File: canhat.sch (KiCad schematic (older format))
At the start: 27 parts, among them J1 Raspberry_Pi_2_3, J2 CAN In/Out/GND, J3 5V, U1 MCP2515-xSO, U2 SN65HVD234, U3 AT24C32-SSHM, Y1 16MHz

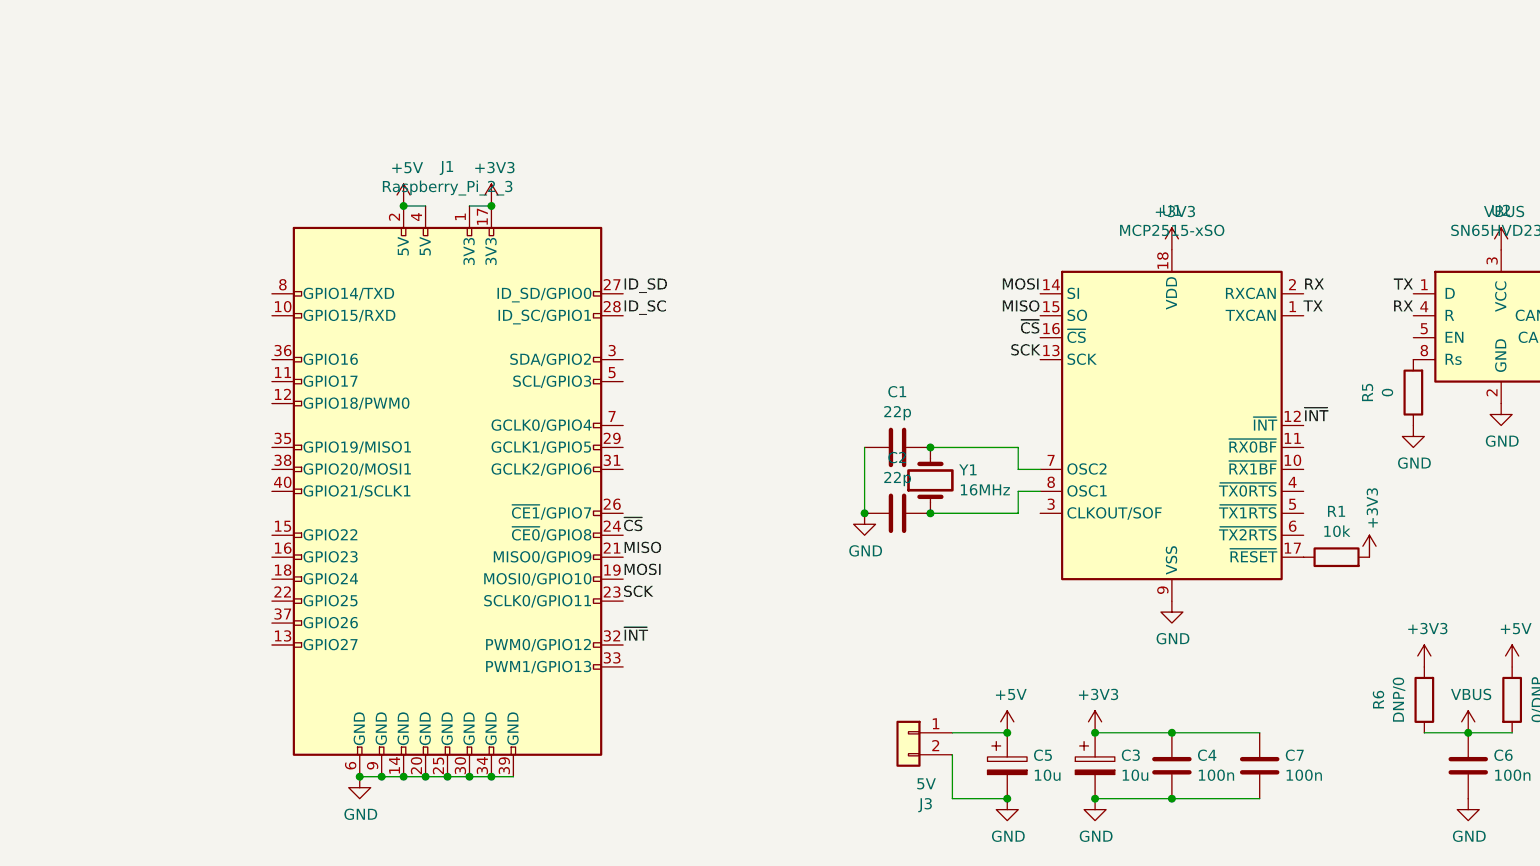
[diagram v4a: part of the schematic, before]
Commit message: Added protective resistors between xceiver and controller
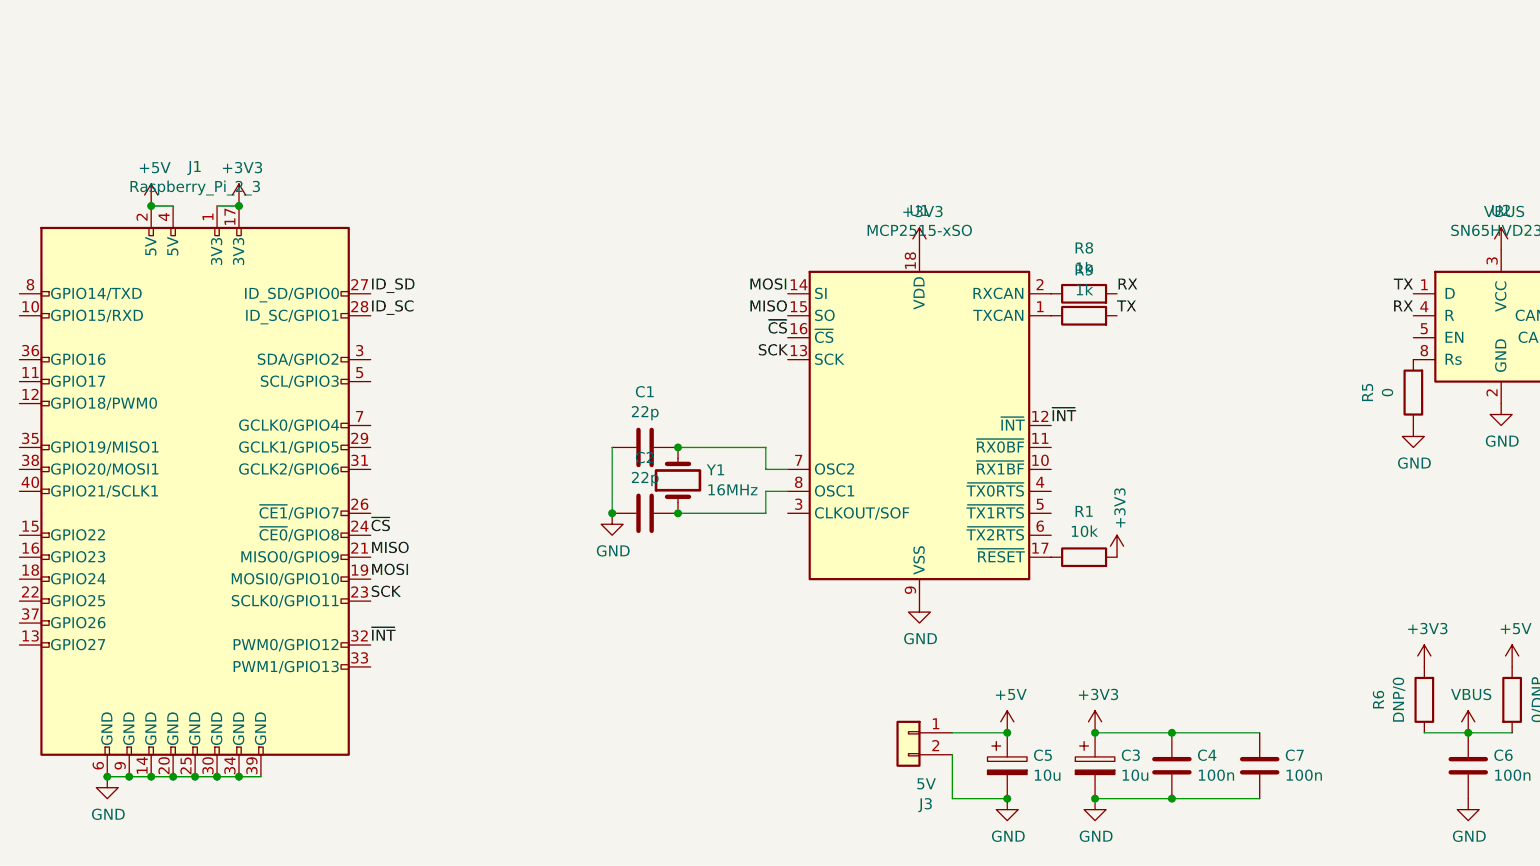
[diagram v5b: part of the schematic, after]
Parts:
- added R8, R9: 1k, Resistor_SMD:R_0805_2012Metric_Pad1.15x1.40mm_HandSolder, symbol Device:R
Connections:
- net RX: now also R8.2; no longer U1.2 (RXCAN)
- net TX: now also R9.2; no longer U1.1 (TXCAN)
- new net: R9.1, U1.1 (TXCAN)
- new net: R8.1, U1.2 (RXCAN)
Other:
- moved on the sheet: C1, C2, J1, R1, U1, Y1

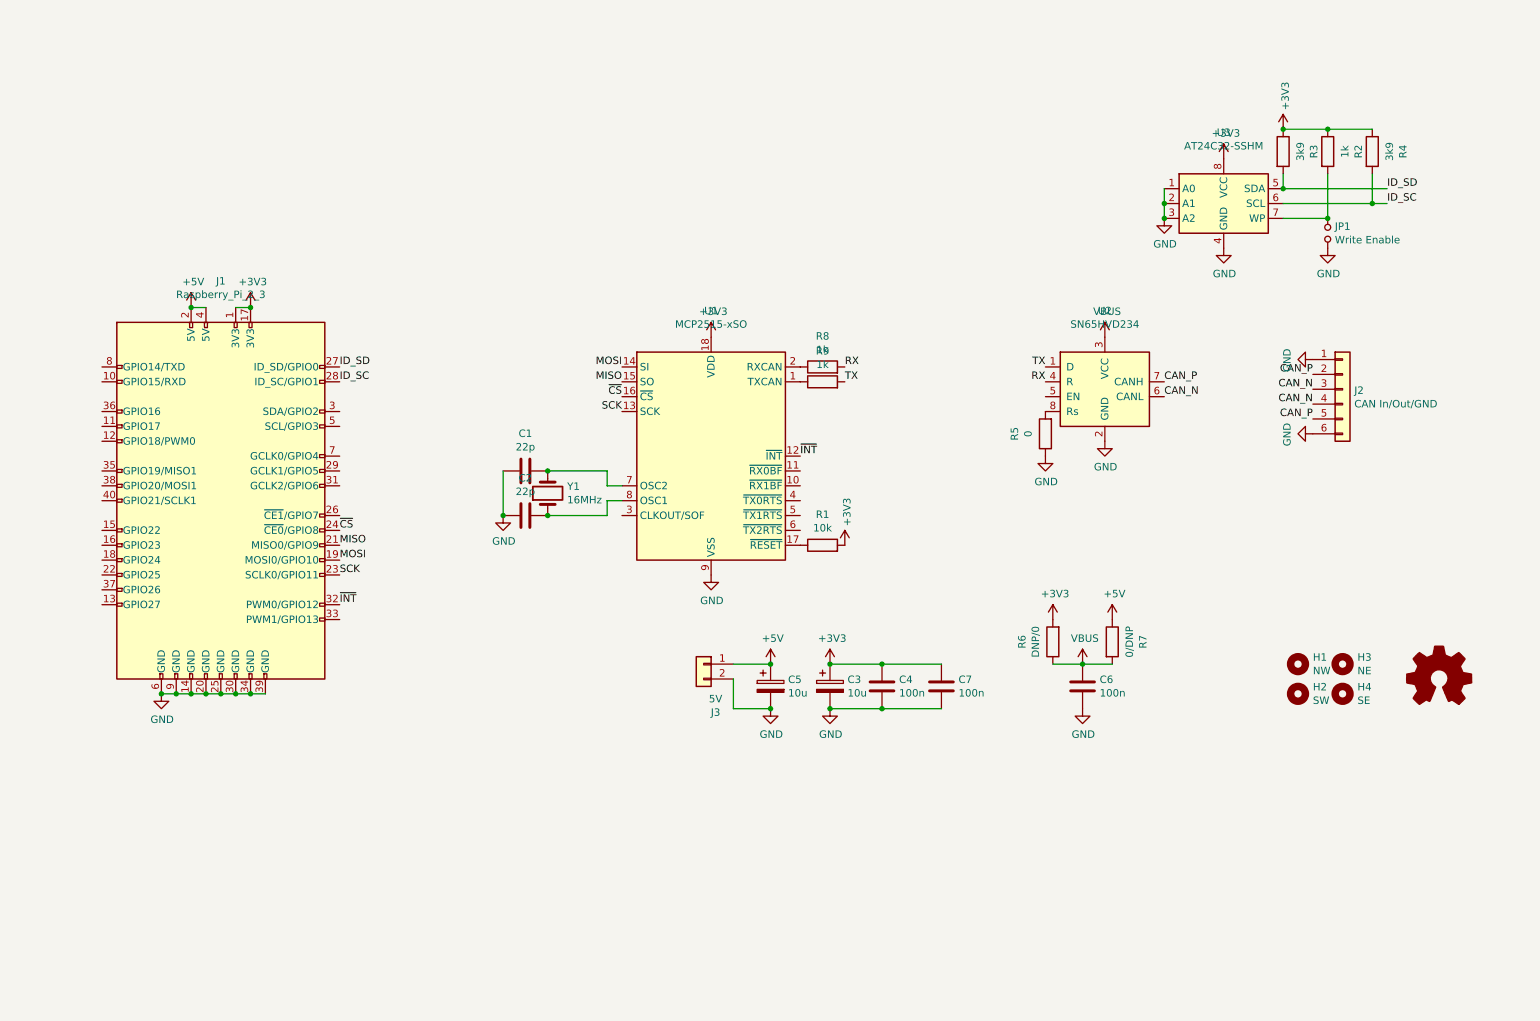
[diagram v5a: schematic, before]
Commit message: Added 12V step-down power supply
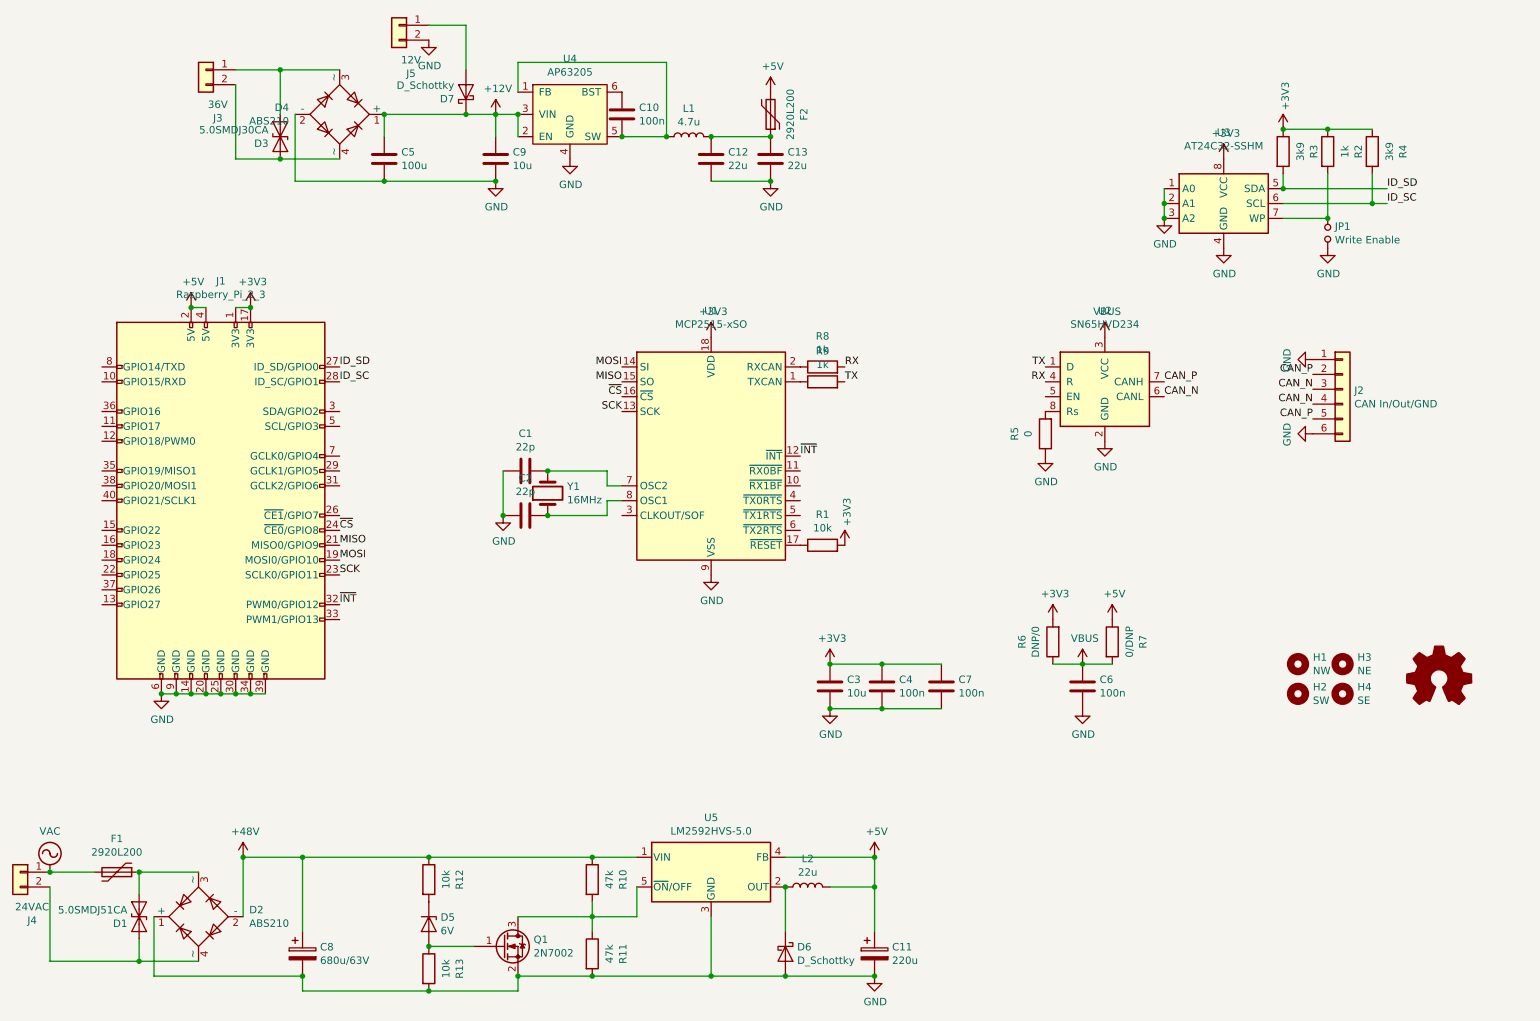
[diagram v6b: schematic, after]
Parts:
- removed C3, C5: 10u, Capacitor_Tantalum_SMD:CP_EIA-7343-31_Kemet-D_Pad2.25x2.55mm_HandSolder, symbol Device:CP
- added C10: 100n, Capacitor_SMD:C_0805_2012Metric_Pad1.15x1.40mm_HandSolder, symbol Device:C
- added C11: 220u, symbol Device:CP
- added C12, C13: 22u, Capacitor_SMD:C_0805_2012Metric_Pad1.15x1.40mm_HandSolder, symbol Device:C
- added C3: 10u, Capacitor_Tantalum_SMD:CP_EIA-7343-31_Kemet-D_Pad2.25x2.55mm_HandSolder, symbol Device:C
- added C5: 100u, symbol Device:C
- added C8: 680u/63V, Capacitor_Tantalum_SMD:CP_EIA-7343-31_Kemet-D_Pad2.25x2.55mm_HandSolder, symbol Device:CP
- added C9: 10u, Capacitor_SMD:C_1210_3225Metric_Pad1.42x2.65mm_HandSolder, symbol Device:C
- added D1: 5.0SMDJ51CA, symbol Device:D_TVS
- added D2: ABS210, symbol Diode_Bridge:ABS2
- added D3: 5.0SMDJ30CA, Diode_SMD:D_SMC_Handsoldering, symbol Device:D_TVS
- added D4: ABS210, Diode_SMD:Diode_Bridge_Diotec_ABS, symbol Diode_Bridge:ABS2
- added D5: 6V, symbol Device:D_Zener
- added D6: D_Schottky, symbol Device:D_Schottky
- added D7: D_Schottky, Diode_SMD:D_SMA_Handsoldering, symbol Device:D_Schottky
- added F1: 2920L200, symbol Device:Polyfuse
- added F2: 2920L200, Fuse:Fuse_2920_7451Metric_Pad2.10x5.45mm_HandSolder, symbol Device:Polyfuse
- added J4: 24VAC, TerminalBlock_TE-Connectivity:TerminalBlock_TE_282834-2_1x02_P2.54mm_Horizontal, symbol Connector_Generic:Conn_01x02
- added J5: 12V, TerminalBlock_TE-Connectivity:TerminalBlock_TE_282834-2_1x02_P2.54mm_Horizontal, symbol Connector_Generic:Conn_01x02
- added L1: 4.7u, Inductor_SMD:L_Abracon_ASPI-0630LR, symbol Device:L
- added L2: 22u, symbol Device:L
- added Q1: 2N7002, Package_TO_SOT_SMD:SOT-23, symbol Transistor_FET:2N7002
- added R10, R11: 47k, Resistor_SMD:R_0805_2012Metric_Pad1.15x1.40mm_HandSolder, symbol Device:R
- added R12, R13: 10k, Resistor_SMD:R_0805_2012Metric_Pad1.15x1.40mm_HandSolder, symbol Device:R
- added U4: AP63205, Package_TO_SOT_SMD:TSOT-23-6, symbol oni:AP63205
- added U5: LM2592HVS-5.0, Package_TO_SOT_SMD:TO-263-5_TabPin3, symbol oni:LM2592HVS-5.0
- J3: value 5V -> 36V
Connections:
- net +3V3: now also C3.1
- net +5V: now also C11.1, F2.2, L2.2, U5.4 (FB); no longer J3.1 (Pin_1)
- net GND: now also C11.2, C12.2, C13.2, C3.2, C5.2, C8.2, C9.2, D2.1 (+), D4.2 (-), D6.2 (A), J5.2 (Pin_2), Q1.2 (S), R11.2, R13.2, U4.4 (GND), U5.3 (GND); no longer J3.2 (Pin_2)
- new net: Q1.3 (D), R10.2, R11.1, U5.5 (~ON~/OFF)
- new net: D1.1 (A1), D2.4 (~~), J4.2 (Pin_2)
- new net: D1.2 (A2), D2.3 (~~), F1.1
- new net: D6.1 (K), L2.1, U5.2 (OUT)
- new net: D5.2 (A), Q1.1 (G), R13.1
- new net: D5.1 (K), R12.2
- new net: C12.1, C13.1, F2.1, L1.2
- new net: C10.2, L1.1, U4.1 (FB), U4.5 (SW)
- new net: C10.1, U4.6 (BST)
- new net: D3.1 (A1), D4.4 (~~), J3.2 (Pin_2)
- new net: D3.2 (A2), D4.3 (~~), J3.1 (Pin_1)
- new net: D7.2 (A), J5.1 (Pin_1)
- new net +12V: C5.1, C9.1, D4.1 (+), D7.1 (K), U4.2 (EN), U4.3 (VIN)
- new net +48V: C8.1, D2.2 (-), R10.1, R12.1, U5.1 (VIN)
- new net VAC: F1.2, J4.1 (Pin_1)

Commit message: Removed obsolete PSU and added missing 3.3V cap
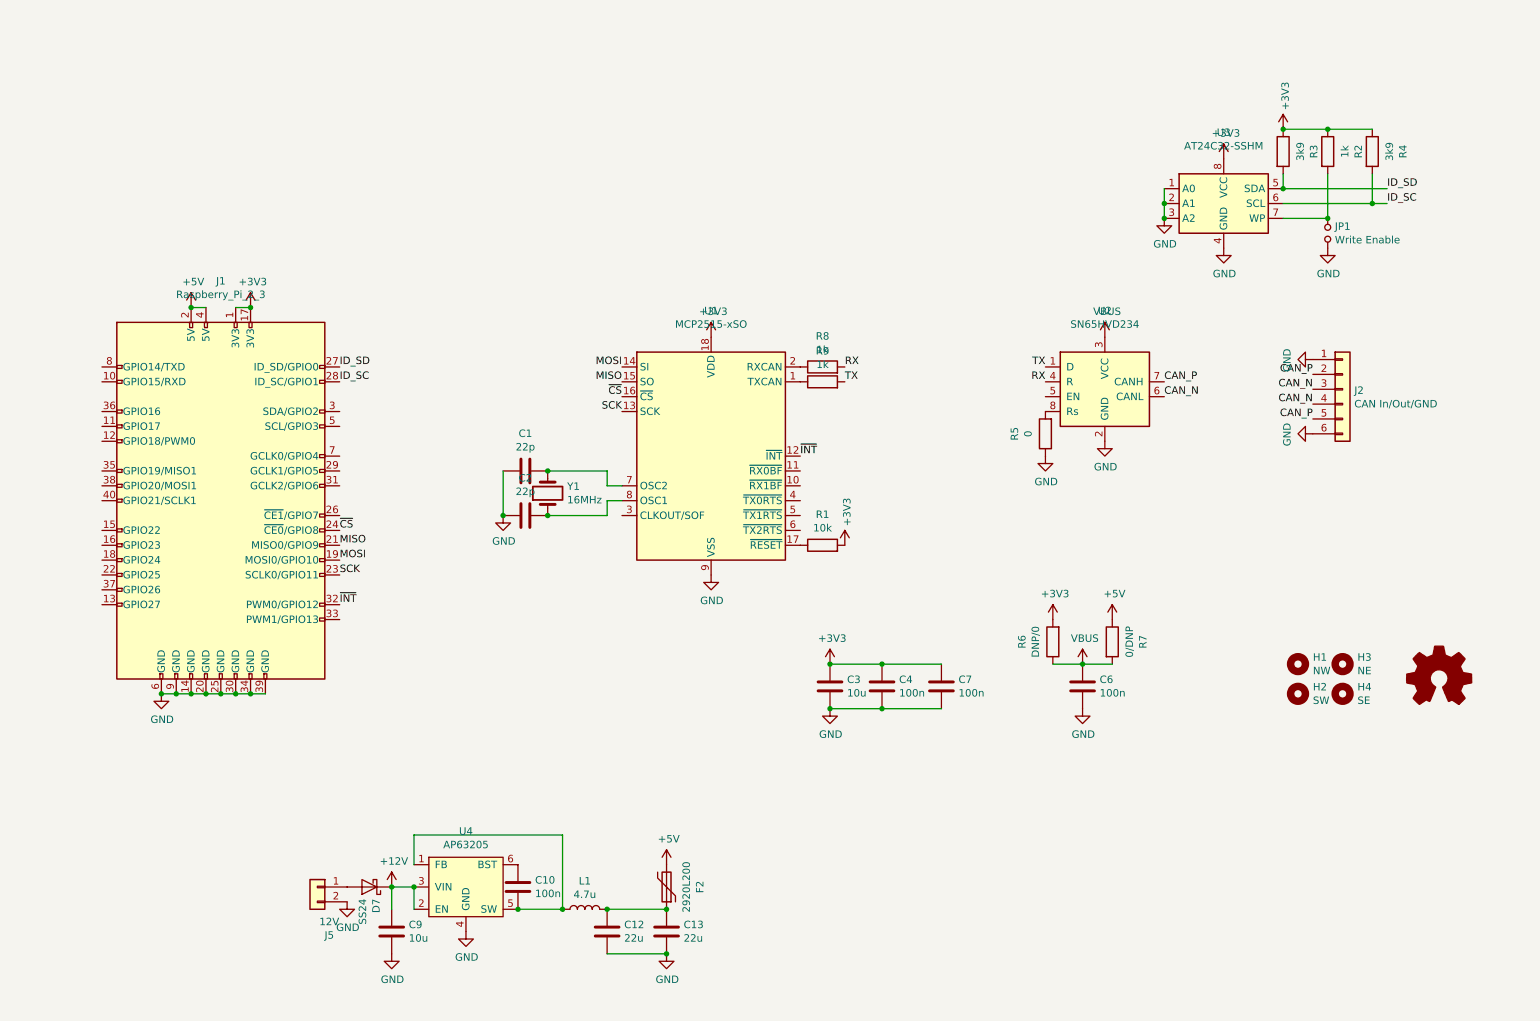
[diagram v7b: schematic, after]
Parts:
- removed C11: 220u, symbol Device:CP
- removed C5: 100u, symbol Device:C
- removed C8: 680u/63V, Capacitor_Tantalum_SMD:CP_EIA-7343-31_Kemet-D_Pad2.25x2.55mm_HandSolder, symbol Device:CP
- removed D1: 5.0SMDJ51CA, symbol Device:D_TVS
- removed D2: ABS210, symbol Diode_Bridge:ABS2
- removed D3: 5.0SMDJ30CA, Diode_SMD:D_SMC_Handsoldering, symbol Device:D_TVS
- removed D4: ABS210, Diode_SMD:Diode_Bridge_Diotec_ABS, symbol Diode_Bridge:ABS2
- removed D5: 6V, symbol Device:D_Zener
- removed D6: D_Schottky, symbol Device:D_Schottky
- removed F1: 2920L200, symbol Device:Polyfuse
- removed J3: 36V, TerminalBlock_TE-Connectivity:TerminalBlock_TE_282834-2_1x02_P2.54mm_Horizontal, symbol Connector_Generic:Conn_01x02
- removed J4: 24VAC, TerminalBlock_TE-Connectivity:TerminalBlock_TE_282834-2_1x02_P2.54mm_Horizontal, symbol Connector_Generic:Conn_01x02
- removed L2: 22u, symbol Device:L
- removed Q1: 2N7002, Package_TO_SOT_SMD:SOT-23, symbol Transistor_FET:2N7002
- removed R10, R11: 47k, Resistor_SMD:R_0805_2012Metric_Pad1.15x1.40mm_HandSolder, symbol Device:R
- removed R12, R13: 10k, Resistor_SMD:R_0805_2012Metric_Pad1.15x1.40mm_HandSolder, symbol Device:R
- removed U5: LM2592HVS-5.0, Package_TO_SOT_SMD:TO-263-5_TabPin3, symbol oni:LM2592HVS-5.0
- C3: footprint Capacitor_Tantalum_SMD:CP_EIA-7343-31_Kemet-D_Pad2.25x2.55mm_HandSolder -> Capacitor_SMD:C_1210_3225Metric_Pad1.42x2.65mm_HandSolder
- D7: value D_Schottky -> SS24
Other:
- moved on the sheet: C10, C12, C13, C9, D7, F2, J5, L1, U4

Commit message: Routing and tweaking
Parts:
- L1: footprint Inductor_SMD:L_Abracon_ASPI-0630LR -> onitake:DS75LC
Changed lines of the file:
@@
 F 0 "L1" V 4690 6850 50  0000 C CNN
 F 1 "4.7u" V 4599 6850 50  0000 C CNN
-F 2 "Inductor_SMD:L_Abracon_ASPI-0630LR" H 4500 6850 50  0001 C CNN
+F 2 "onitake:DS75LC" H 4500 6850 50  0001 C CNN
 F 3 "~" H 4500 6850 50  0001 C CNN
 	1    4500 6850
